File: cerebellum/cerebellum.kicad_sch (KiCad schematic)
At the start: 25 parts, among them J1 GPIO, J2 Conn_MOTA, J3 Conn_MOTB, J4 MD_POW, J5 Conn_SPI, J6 Conn_UART, J7 Conn_I2C, J8 VBUS(OUT), SW1 SW_PULLUP, SW2 SW_PULLDOWN, SW3 SW_SPDT, U1 CAT24C256, U2 POLOLU_TB6612_CARRIER, U3 HC-SR04

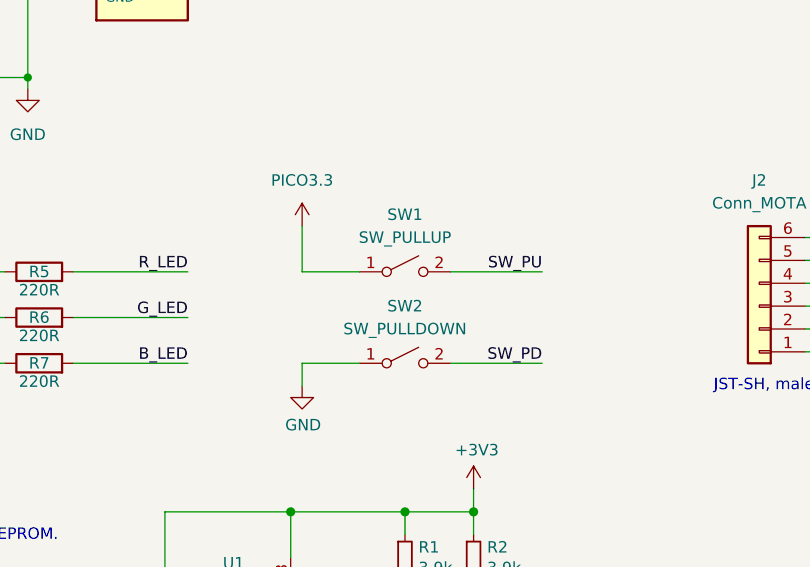
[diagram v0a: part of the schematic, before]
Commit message: update schematic and pcb
assigned footprints
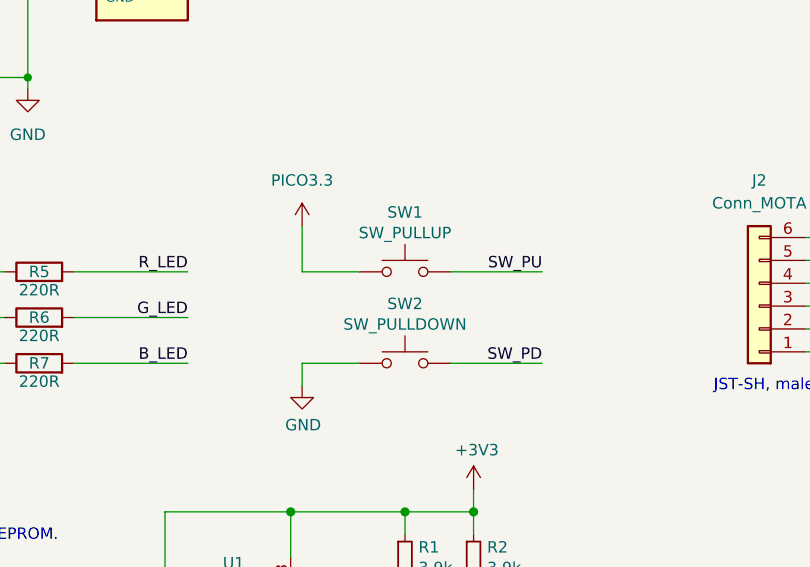
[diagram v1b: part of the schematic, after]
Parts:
- removed SW1: SW_PULLUP, symbol Switch:SW_SPST
- removed SW2: SW_PULLDOWN, symbol Switch:SW_SPST
- added SW1: SW_PULLUP, Button_Switch_THT:SW_PUSH_6mm_H5mm, symbol Switch:SW_Push
- added SW2: SW_PULLDOWN, Button_Switch_THT:SW_PUSH_6mm_H5mm, symbol Switch:SW_Push
- C1: footprint POLOLU_TB6612:POLOLU_TB6612 -> (none)
- D1: footprint (none) -> LED_THT:LED_D5.0mm-4_RGB
- J2, J3: footprint (none) -> Connector_JST:JST_SH_BM06B-SRSS-TB_1x06-1MP_P1.00mm_Vertical
- J4: footprint (none) -> Connector_PinHeader_2.54mm:PinHeader_1x02_P2.54mm_Horizontal
- J5: footprint (none) -> Connector_PinHeader_2.54mm:PinHeader_1x04_P2.54mm_Vertical
- J6, J7, J8: footprint (none) -> Connector_PinHeader_2.54mm:PinHeader_1x02_P2.54mm_Vertical
- R3, R4: footprint (none) -> Resistor_SMD:R_1206_3216Metric_Pad1.30x1.75mm_HandSolder
- R5, R6, R7: footprint (none) -> Resistor_THT:R_Axial_DIN0207_L6.3mm_D2.5mm_P10.16mm_Horizontal
- SW3: footprint (none) -> Button_Switch_THT:SW_E-Switch_EG1271_SPDT
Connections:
- net GND: now also SW2.1
- net PICO3.3: now also SW1.1
- net SW_PD: now also SW2.2
- net SW_PU: now also SW1.2
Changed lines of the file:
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@@
 			)
 		)
-		(property "Footprint" ""
+		(property "Footprint" "Resistor_SMD:R_1206_3216Metric_Pad1.30x1.75mm_HandSolder"
 			(at 43.18 107.188 90)
 			(effects
@@
 			)
 		)
-		(property "Footprint" ""
+		(property "Footprint" "Connector_PinHeader_2.54mm:PinHeader_1x04_P2.54mm_Vertical"
 			(at 195.58 107.95 0)
 			(effects
@@
 			)
 		)
-		(property "Footprint" "POLOLU_TB6612:POLOLU_TB6612"
+		(property "Footprint" ""
 			(at 67.31 177.8 0)
 			(effects
@@
 			)
 		)
-		(property "Footprint" ""
+		(property "Footprint" "Connector_JST:JST_SH_BM06B-SRSS-TB_1x06-1MP_P1.00mm_Vertical"
 			(at 163.83 142.24 0)
 			(effects
@@
 			)
 		)
-		(property "Footprint" ""
+		(property "Footprint" "Connector_PinHeader_2.54mm:PinHeader_1x02_P2.54mm_Horizontal"
 			(at 44.45 33.02 0)
 			(effects
@@
 	)
 	(symbol
-		(lib_id "Switch:SW_SPST")
-		(at 93.98 138.43 0)
-		(unit 1)
-		(exclude_from_sim no)
-		(in_bom yes)
-		(on_board yes)
-		(dnp no)
-		(fields_autoplaced yes)
-		(property "Reference" "SW1"
-			(at 93.98 132.08 0)
-			(effects
-				(font
-					(size 1.27 1.27)
-				)
-			)
-		)
-		(property "Value" "SW_PULLUP"
-			(at 93.98 134.62 0)
-			(effects
-				(font
-					(size 1.27 1.27)
-				)
-			)
-		)
-		(property "Footprint" ""
-			(at 93.98 138.43 0)
-			(effects
-				(font
-					(size 1.27 1.27)
-				)
-				(hide yes)
-			)
-		)
-		(property "Datasheet" "~"
-			(at 93.98 138.43 0)
-			(effects
-				(font
-					(size 1.27 1.27)
-				)
-				(hide yes)
-			)
-		)
-		(property "Description" "Single Pole Single Throw (SPST) switch"
-			(at 93.98 138.43 0)
-			(effects
-				(font
-					(size 1.27 1.27)
-				)
-				(hide yes)
-			)
-		)
-		(pin "2"
-		)
-		(pin "1"
-		)
-		(instances
-			(project ""
-				(path "/e63e39d7-6ac0-4ffd-8aa3-1841a4541b55"
-					(reference "SW1")
-					(unit 1)
-				)
-			)
-		)
-	)
-	(symbol
 		(lib_id "Device:R")
 		(at 53.34 138.43 90)
@@
 			)
 		)
-		(property "Footprint" ""
+		(property "Footprint" "Resistor_THT:R_Axial_DIN0207_L6.3mm_D2.5mm_P10.16mm_Horizontal"
 			(at 53.34 140.208 90)
 			(effects
@@
 			)
 		)
-		(property "Footprint" ""
+		(property "Footprint" "Resistor_THT:R_Axial_DIN0207_L6.3mm_D2.5mm_P10.16mm_Horizontal"
 			(at 53.34 145.288 90)
 			(effects
@@
 	)
 	(symbol
+		(lib_id "Switch:SW_Push")
+		(at 93.98 138.43 0)
+		(unit 1)
+		(exclude_from_sim no)
+		(in_bom yes)
+		(on_board yes)
+		(dnp no)
+		(property "Reference" "SW1"
+			(at 93.98 131.826 0)
+			(effects
+				(font
+					(size 1.27 1.27)
+				)
+			)
+		)
+		(property "Value" "SW_PULLUP"
+			(at 93.98 134.112 0)
+			(effects
+				(font
+					(size 1.27 1.27)
+				)
+			)
+		)
+		(property "Footprint" "Button_Switch_THT:SW_PUSH_6mm_H5mm"
+			(at 93.98 133.35 0)
+			(effects
+				(font
+					(size 1.27 1.27)
+				)
+				(hide yes)
+			)
+		)
+		(property "Datasheet" "~"
+			(at 93.98 133.35 0)
+			(effects
+				(font
+					(size 1.27 1.27)
+				)
+				(hide yes)
+			)
+		)
+		(property "Description" "Push button switch, generic, two pins"
+			(at 93.98 138.43 0)
+			(effects
+				(font
+					(size 1.27 1.27)
+				)
+				(hide yes)
+			)
+		)
+		(pin "2"
+		)
+		(pin "1"
+		)
+		(instances
+			(project ""
+				(path "/e63e39d7-6ac0-4ffd-8aa3-1841a4541b55"
+					(reference "SW1")
+					(unit 1)
+				)
+			)
+		)
+	)
+	(symbol
 		(lib_name "GND_1")
 		(lib_id "power:GND")
@@
 			)
 		)
-		(property "Footprint" ""
+		(property "Footprint" "LED_THT:LED_D5.0mm-4_RGB"
 			(at 38.1 144.78 0)
 			(effects
@@
 			)
 		)
-		(property "Footprint" ""
+		(property "Footprint" "Connector_PinHeader_2.54mm:PinHeader_1x02_P2.54mm_Vertical"
 			(at 223.52 105.41 0)
 			(effects
@@
 			)
 		)
-		(property "Footprint" ""
+		(property "Footprint" "Connector_PinHeader_2.54mm:PinHeader_1x02_P2.54mm_Vertical"
 			(at 167.64 21.59 0)
 			(effects
@@
 	)
 	(symbol
-		(lib_id "Switch:SW_SPST")
-		(at 93.98 148.59 0)
-		(unit 1)
-		(exclude_from_sim no)
-		(in_bom yes)
-		(on_board yes)
-		(dnp no)
-		(fields_autoplaced yes)
-		(property "Reference" "SW2"
-			(at 93.98 142.24 0)
-			(effects
-				(font
-					(size 1.27 1.27)
-				)
-			)
-		)
-		(property "Value" "SW_PULLDOWN"
-			(at 93.98 144.78 0)
-			(effects
-				(font
-					(size 1.27 1.27)
-				)
-			)
-		)
-		(property "Footprint" ""
-			(at 93.98 148.59 0)
-			(effects
-				(font
-					(size 1.27 1.27)
-				)
-				(hide yes)
-			)
-		)
-		(property "Datasheet" "~"
-			(at 93.98 148.59 0)
-			(effects
-				(font
-					(size 1.27 1.27)
-				)
-				(hide yes)
-			)
-		)
-		(property "Description" "Single Pole Single Throw (SPST) switch"
-			(at 93.98 148.59 0)
-			(effects
-				(font
-					(size 1.27 1.27)
-				)
-				(hide yes)
-			)
-		)
-		(pin "1"
-		)
-		(pin "2"
-		)
-		(instances
-			(project ""
-				(path "/e63e39d7-6ac0-4ffd-8aa3-1841a4541b55"
-					(reference "SW2")
-					(unit 1)
-				)
-			)
-		)
-	)
-	(symbol
 		(lib_id "Device:R")
 		(at 33.02 111.76 0)
@@
 			)
 		)
-		(property "Footprint" ""
+		(property "Footprint" "Resistor_SMD:R_1206_3216Metric_Pad1.30x1.75mm_HandSolder"
 			(at 31.242 111.76 90)
 			(effects
@@
 			)
 		)
-		(property "Footprint" ""
+		(property "Footprint" "Resistor_THT:R_Axial_DIN0207_L6.3mm_D2.5mm_P10.16mm_Horizontal"
 			(at 53.34 150.368 90)
 			(effects
@@
 			)
 		)
-		(property "Footprint" ""
+		(property "Footprint" "Connector_JST:JST_SH_BM06B-SRSS-TB_1x06-1MP_P1.00mm_Vertical"
 			(at 133.35 142.24 0)
 			(effects
@@
 	)
 	(symbol
+		(lib_id "Switch:SW_Push")
+		(at 93.98 148.59 0)
+		(unit 1)
+		(exclude_from_sim no)
+		(in_bom yes)
+		(on_board yes)
+		(dnp no)
+		(property "Reference" "SW2"
+			(at 93.98 141.986 0)
+			(effects
+				(font
+					(size 1.27 1.27)
+				)
+			)
+		)
+		(property "Value" "SW_PULLDOWN"
+			(at 93.98 144.272 0)
+			(effects
+				(font
+					(size 1.27 1.27)
+				)
+			)
+		)
+		(property "Footprint" "Button_Switch_THT:SW_PUSH_6mm_H5mm"
+			(at 93.98 143.51 0)
+			(effects
+				(font
+					(size 1.27 1.27)
+				)
+				(hide yes)
+			)
+		)
+		(property "Datasheet" "~"
+			(at 93.98 143.51 0)
+			(effects
+				(font
+					(size 1.27 1.27)
+				)
+				(hide yes)
+			)
+		)
+		(property "Description" "Push button switch, generic, two pins"
+			(at 93.98 148.59 0)
+			(effects
+				(font
+					(size 1.27 1.27)
+				)
+				(hide yes)
+			)
+		)
+		(pin "2"
+		)
+		(pin "1"
+		)
+		(instances
+			(project "cerebellum"
+				(path "/e63e39d7-6ac0-4ffd-8aa3-1841a4541b55"
+					(reference "SW2")
+					(unit 1)
+				)
+			)
+		)
+	)
+	(symbol
 		(lib_id "power:GND")
 		(at 175.26 152.4 0)
@@
 			)
 		)
-		(property "Footprint" ""
+		(property "Footprint" "Button_Switch_THT:SW_E-Switch_EG1271_SPDT"
 			(at 106.68 29.21 0)
 			(effects
@@
 			)
 		)
-		(property "Footprint" ""
+		(property "Footprint" "Connector_PinHeader_2.54mm:PinHeader_1x02_P2.54mm_Vertical"
 			(at 254 105.41 0)
 			(effects

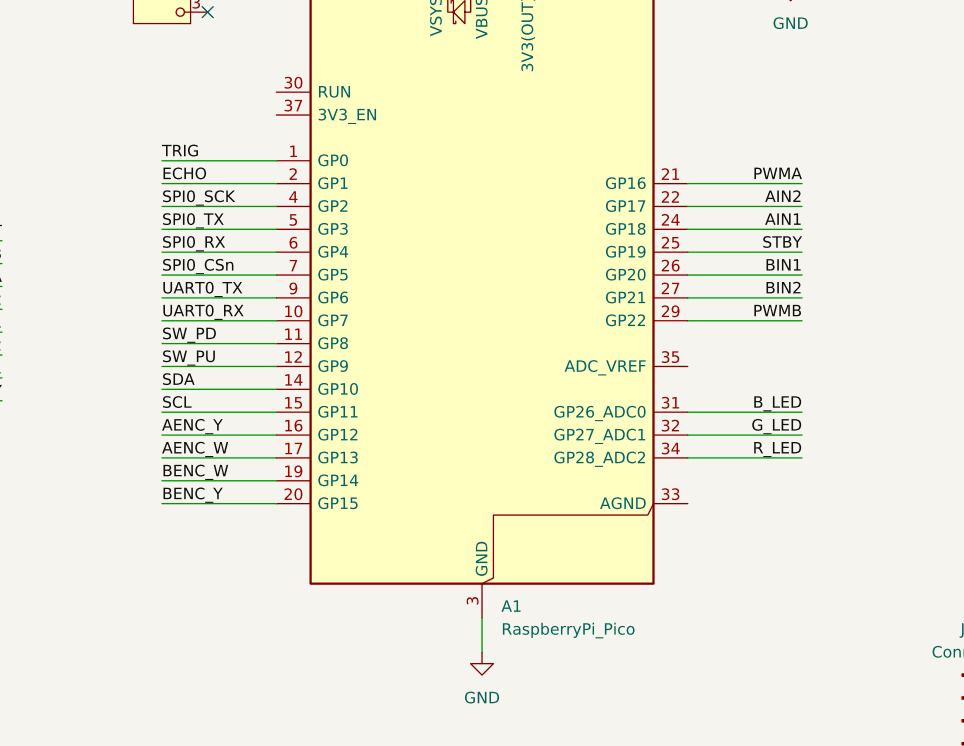
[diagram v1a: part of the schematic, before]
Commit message: update md wiring
split motor a and b to two sides
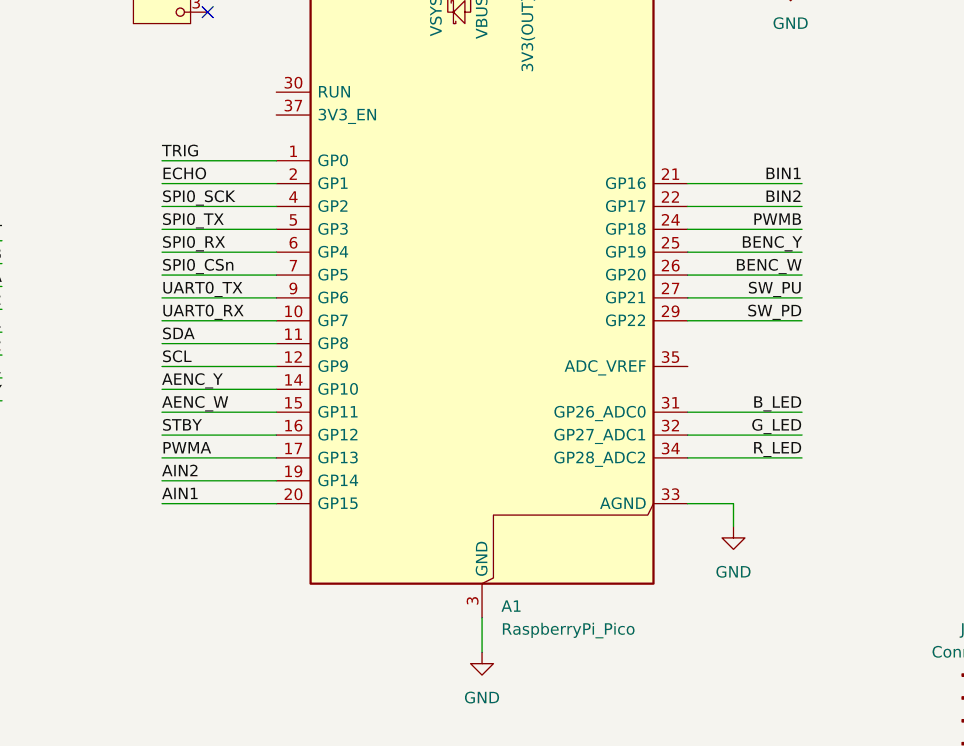
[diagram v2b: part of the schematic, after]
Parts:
- A1: footprint Module:RaspberryPi_Pico_Common_THT -> RaspberryPi_Pico:RaspberryPi_Pico_Common_THT
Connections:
- net AENC_W: now also A1.15 (GP11); no longer A1.17 (GP13)
- net AENC_Y: now also A1.14 (GP10); no longer A1.16 (GP12)
- net AIN1: now also A1.20 (GP15); no longer A1.24 (GP18)
- net AIN2: now also A1.19 (GP14); no longer A1.22 (GP17)
- net BENC_W: now also A1.26 (GP20); no longer A1.19 (GP14)
- net BENC_Y: now also A1.25 (GP19); no longer A1.20 (GP15)
- net BIN1: now also A1.21 (GP16); no longer A1.26 (GP20)
- net BIN2: now also A1.22 (GP17); no longer A1.27 (GP21)
- net GND: now also A1.33 (AGND)
- net PWMA: now also A1.17 (GP13); no longer A1.21 (GP16)
- net PWMB: now also A1.24 (GP18); no longer A1.29 (GP22)
- net SCL: now also A1.12 (GP9); no longer A1.15 (GP11)
- net SDA: now also A1.11 (GP8); no longer A1.14 (GP10)
- net STBY: now also A1.16 (GP12); no longer A1.25 (GP19)
- net SW_PD: now also A1.29 (GP22); no longer A1.11 (GP8)
- net SW_PU: now also A1.27 (GP21); no longer A1.12 (GP9)
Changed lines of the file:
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@@
 	(wire
 		(pts
+			(xy 165.1 86.36) (xy 170.18 86.36)
+		)
+		(stroke
+			(width 0)
+			(type default)
+		)
+	)
+	(wire
+		(pts
 			(xy 246.38 66.04) (xy 273.05 66.04)
 		)
@@
 	(wire
 		(pts
+			(xy 170.18 86.36) (xy 170.18 88.9)
+		)
+		(stroke
+			(width 0)
+			(type default)
+		)
+	)
+	(wire
+		(pts
 			(xy 248.92 63.5) (xy 246.38 63.5)
 		)
@@
 		)
 	)
-	(label "STBY"
-		(at 177.8 58.42 180)
-		(effects
-			(font
-				(size 1.27 1.27)
-			)
-			(justify right bottom)
-		)
-	)
 	(label "ID_SDA"
 		(at 204.47 60.96 0)
@@
 		)
 	)
-	(label "PWMA"
-		(at 177.8 50.8 180)
-		(effects
-			(font
-				(size 1.27 1.27)
-			)
-			(justify right bottom)
-		)
-	)
-	(label "AIN2"
-		(at 177.8 53.34 180)
-		(effects
-			(font
-				(size 1.27 1.27)
-			)
-			(justify right bottom)
-		)
-	)
 	(label "AENC_Y"
 		(at 149.86 142.24 180)
@@
 		)
 	)
-	(label "BENC_W"
-		(at 106.68 83.82 0)
-		(effects
-			(font
-				(size 1.27 1.27)
-			)
-			(justify left bottom)
-		)
-	)
 	(label "ID_SDA"
 		(at 110.49 175.26 180)
@@
 		)
 	)
+	(label "BENC_W"
+		(at 177.8 60.96 180)
+		(effects
+			(font
+				(size 1.27 1.27)
+			)
+			(justify right bottom)
+		)
+	)
 	(label "GPIO21{slash}PCM.DOUT"
 		(at 273.05 76.2 180)
@@
 		)
 	)
-	(label "BIN1"
-		(at 177.8 60.96 180)
+	(label "MISO"
+		(at 204.47 53.34 0)
 		(effects
 			(font
 				(size 1.27 1.27)
 			)
-			(justify right bottom)
+			(justify left bottom)
 		)
 	)
-	(label "MISO"
-		(at 204.47 53.34 0)
+	(label "SPI0_CSn"
+		(at 213.36 113.03 180)
 		(effects
 			(font
 				(size 1.27 1.27)
 			)
-			(justify left bottom)
+			(justify right bottom)
 		)
 	)
-	(label "SPI0_CSn"
-		(at 213.36 113.03 180)
+	(label "BENC_Y"
+		(at 177.8 58.42 180)
 		(effects
 			(font
@@
 		)
 	)
+	(label "PWMB"
+		(at 177.8 55.88 180)
+		(effects
+			(font
+				(size 1.27 1.27)
+			)
+			(justify right bottom)
+		)
+	)
 	(label "GPIO23"
 		(at 273.05 45.72 180)
@@
 		)
 	)
+	(label "AIN2"
+		(at 106.68 83.82 0)
+		(effects
+			(font
+				(size 1.27 1.27)
+			)
+			(justify left bottom)
+		)
+	)
 	(label "B_LED"
 		(at 69.85 148.59 180)
@@
 		)
 	)
-	(label "SW_PU"
-		(at 106.68 71.12 0)
-		(effects
-			(font
-				(size 1.27 1.27)
-			)
-			(justify left bottom)
-		)
-	)
 	(label "UART0_TX"
 		(at 243.84 105.41 180)
@@
 		)
 	)
-	(label "SDA"
-		(at 106.68 73.66 0)
-		(effects
-			(font
-				(size 1.27 1.27)
-			)
-			(justify left bottom)
-		)
-	)
 	(label "TXD"
 		(at 273.05 35.56 180)
@@
 		)
 	)
-	(label "AIN1"
-		(at 177.8 55.88 180)
+	(label "BIN2"
+		(at 177.8 53.34 180)
 		(effects
 			(font
@@
 	)
 	(label "AENC_W"
-		(at 106.68 81.28 0)
+		(at 106.68 76.2 0)
 		(effects
 			(font
@@
 		)
 	)
+	(label "SW_PD"
+		(at 177.8 66.04 180)
+		(effects
+			(font
+				(size 1.27 1.27)
+			)
+			(justify right bottom)
+		)
+	)
 	(label "PWMB"
 		(at 88.9 59.69 180)
@@
 		)
 	)
-	(label "SW_PD"
-		(at 106.68 68.58 0)
+	(label "SDA"
+		(at 204.47 30.48 0)
 		(effects
 			(font
@@
 		)
 	)
-	(label "SDA"
-		(at 204.47 30.48 0)
+	(label "PWMA"
+		(at 106.68 81.28 0)
 		(effects
 			(font
@@
 		)
 	)
+	(label "AENC_Y"
+		(at 106.68 73.66 0)
+		(effects
+			(font
+				(size 1.27 1.27)
+			)
+			(justify left bottom)
+		)
+	)
 	(label "GPIO25"
 		(at 273.05 53.34 180)
@@
 		)
 	)
+	(label "BIN1"
+		(at 177.8 50.8 180)
+		(effects
+			(font
+				(size 1.27 1.27)
+			)
+			(justify right bottom)
+		)
+	)
 	(label "SCL"
 		(at 204.47 33.02 0)
@@
 		)
 	)
-	(label "PWMB"
-		(at 177.8 66.04 180)
-		(effects
-			(font
-				(size 1.27 1.27)
-			)
-			(justify right bottom)
-		)
-	)
 	(label "SPI0_TX"
 		(at 213.36 107.95 180)
@@
 		)
 	)
-	(label "BIN2"
-		(at 177.8 63.5 180)
-		(effects
-			(font
-				(size 1.27 1.27)
-			)
-			(justify right bottom)
-		)
-	)
 	(label "GPIO12{slash}PWM0"
 		(at 273.05 66.04 180)
@@
 		)
 	)
+	(label "AIN1"
+		(at 106.68 86.36 0)
+		(effects
+			(font
+				(size 1.27 1.27)
+			)
+			(justify left bottom)
+		)
+	)
 	(label "GPIO24"
 		(at 273.05 48.26 180)
@@
 		)
 	)
+	(label "STBY"
+		(at 106.68 78.74 0)
+		(effects
+			(font
+				(size 1.27 1.27)
+			)
+			(justify left bottom)
+		)
+	)
 	(label "SPI0_RX"
 		(at 213.36 110.49 180)
@@
 		)
 	)
+	(label "SDA"
+		(at 106.68 68.58 0)
+		(effects
+			(font
+				(size 1.27 1.27)
+			)
+			(justify left bottom)
+		)
+	)
 	(label "SW_PU"
 		(at 109.22 138.43 180)
@@
 		)
 	)
-	(label "BENC_Y"
-		(at 106.68 86.36 0)
-		(effects
-			(font
-				(size 1.27 1.27)
-			)
-			(justify left bottom)
-		)
-	)
 	(label "TRIG"
 		(at 46.99 102.87 0)
@@
 	)
 	(label "SCL"
-		(at 106.68 76.2 0)
+		(at 106.68 71.12 0)
 		(effects
 			(font
@@
 		)
 	)
-	(label "AENC_Y"
-		(at 106.68 78.74 0)
+	(label "SW_PU"
+		(at 177.8 63.5 180)
 		(effects
 			(font
 				(size 1.27 1.27)
 			)
-			(justify left bottom)
+			(justify right bottom)
 		)
 	)
@@
 			)
 		)
-		(property "Footprint" "Module:RaspberryPi_Pico_Common_THT"
+		(property "Footprint" "RaspberryPi_Pico:RaspberryPi_Pico_Common_THT"
 			(at 142.24 110.49 0)
 			(effects
@@
 					(unit 1)
 				)
+			)
+		)
+	)
+	(symbol
+		(lib_name "GND_1")
+		(lib_id "power:GND")
+		(at 170.18 88.9 0)
+		(unit 1)
+		(exclude_from_sim no)
+		(in_bom yes)
+		(on_board yes)
+		(dnp no)
+		(fields_autoplaced yes)
+		(property "Reference" "#PWR028"
+			(at 170.18 95.25 0)
+			(effects
+				(font
+					(size 1.27 1.27)
+				)
+				(hide yes)
+			)
+		)
+		(property "Value" "GND"
+			(at 170.18 93.98 0)
+			(effects
+				(font
+					(size 1.27 1.27)
+				)
+			)
+		)
+		(property "Footprint" ""
+			(at 170.18 88.9 0)
+			(effects
+				(font
+					(size 1.27 1.27)
+				)
+				(hide yes)
+			)
+		)
+		(property "Datasheet" ""
+			(at 170.18 88.9 0)
+			(effects
+				(font
+					(size 1.27 1.27)
+				)
+				(hide yes)
+			)
+		)
+		(property "Description" "Power symbol creates a global label with name \"GND\" , ground"
+			(at 170.18 88.9 0)
+			(effects
+				(font
+					(size 1.27 1.27)
+				)
+				(hide yes)
+			)
+		)
+		(pin "1"
+		)
+		(instances
+			(project "cerebellum"
+				(path "/e63e39d7-6ac0-4ffd-8aa3-1841a4541b55"
+					(reference "#PWR028")
+					(unit 1)
+				)
